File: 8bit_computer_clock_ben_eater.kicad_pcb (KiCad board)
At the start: 2 copper layers, 28 parts, among them SW1 Step, SW2 Switch, SW3 Halt, U1 LMC555xN, U2 LMC555xN, U3 LMC555xN, U4 74HC00, U5 74HC00

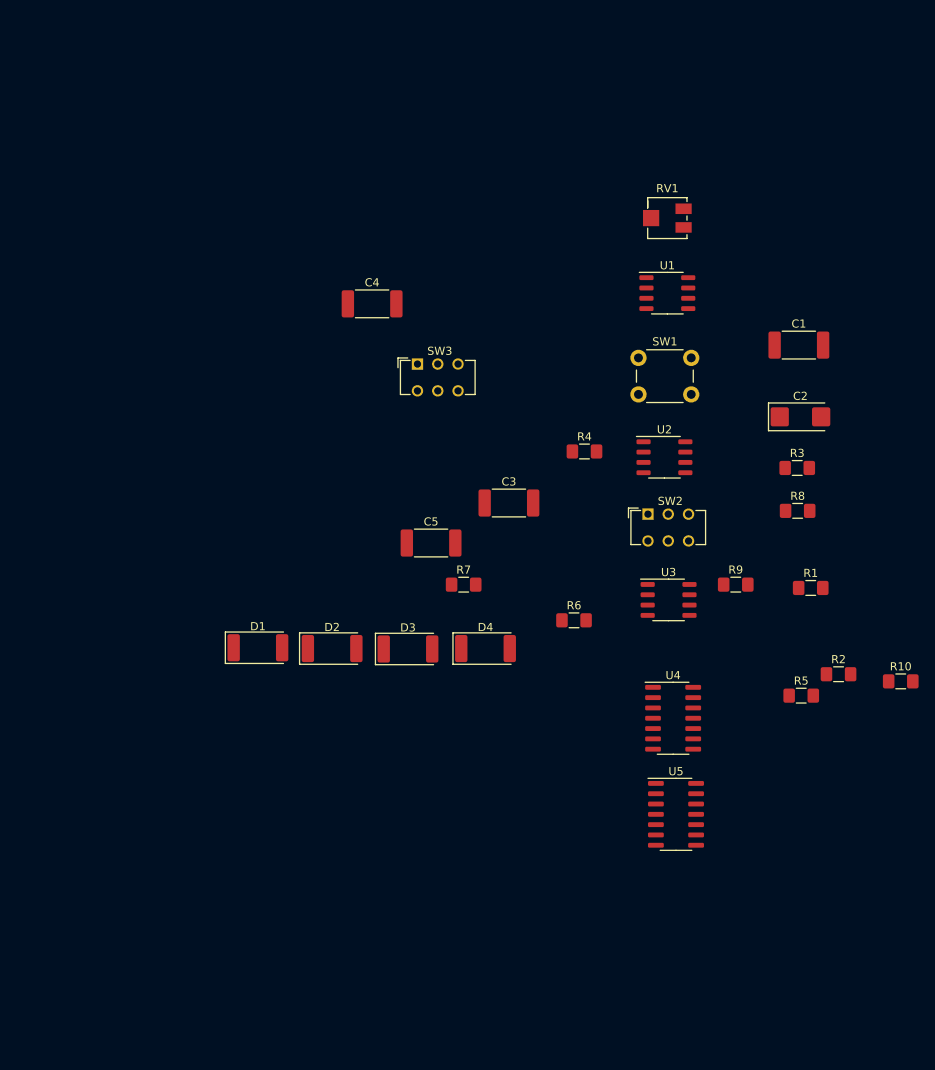
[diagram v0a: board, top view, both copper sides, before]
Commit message: New pcb layout. Added power connection.
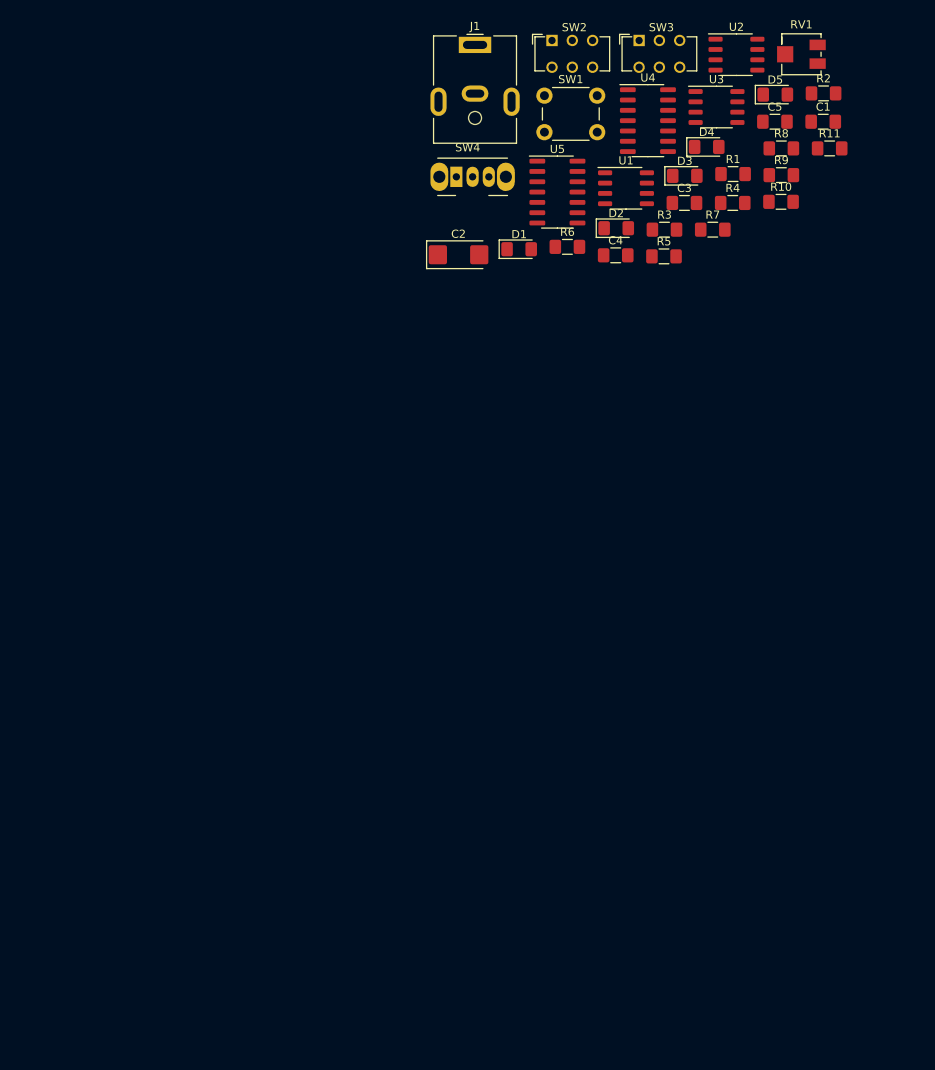
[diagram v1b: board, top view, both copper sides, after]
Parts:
- added D5: LED, LED_SMD:LED_1206_3216Metric_Pad1.42x1.75mm_HandSolder, F.Cu at (187.8, 30.5)
- added J1: Barrel_Jack_MountingPin, Connector_BarrelJack:BarrelJack_CUI_PJ-063AH_Horizontal, F.Cu at (150.8, 24.4)
- added R11: 1k, Resistor_SMD:R_1206_3216Metric_Pad1.42x1.75mm_HandSolder, F.Cu at (194.5, 37.1)
- added SW4: SW_SPDT, Button_Switch_THT:SW_CuK_OS102011MA1QN1_SPDT_Angled, F.Cu at (148.5, 40.6)
- C1, C3, C4, C5: footprint Capacitor_SMD:C_2512_6332Metric_Pad1.52x3.35mm_HandSolder -> Capacitor_SMD:C_1206_3216Metric_Pad1.42x1.75mm_HandSolder
- D1, D2, D3, D4: footprint LED_SMD:LED_2512_6332Metric_Pad1.52x3.35mm_HandSolder -> LED_SMD:LED_1206_3216Metric_Pad1.42x1.75mm_HandSolder
- moved U5 78.0 mm to (161.0, 42.5)
- moved U4 73.7 mm to (172.1, 33.7)
- moved R2 71.6 mm to (193.7, 30.4)
- moved D4 67.5 mm to (179.4, 37.0)
- moved D3 67.5 mm to (176.7, 40.5)
- moved C5 67.0 mm to (187.8, 33.8)
- moved D2 62.5 mm to (168.2, 47.0)
- moved U3 61.0 mm to (180.6, 32.0)
- moved R10 60.9 mm to (188.5, 43.7)
- moved SW2 59.5 mm to (160.3, 23.8)
- moved D1 58.7 mm to (156.2, 49.6)
- moved R5 56.7 mm to (174.1, 50.4)
- moved R7 53.4 mm to (180.1, 47.1)
- moved R1 51.9 mm to (182.6, 40.3)
- moved R9 50.8 mm to (188.5, 40.4)
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
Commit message: Changed all footprints to SMD/SMT. Used a 556 instead of two 555. Beginning of a PCB.
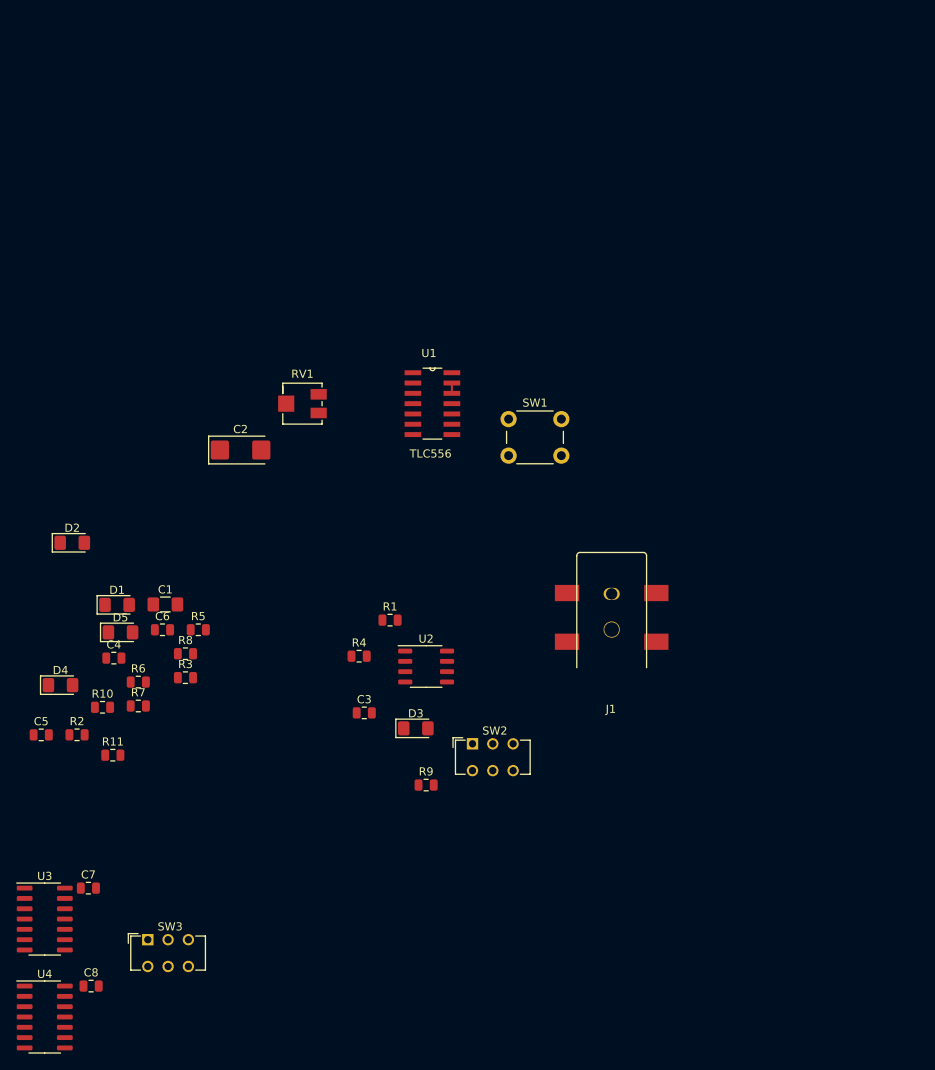
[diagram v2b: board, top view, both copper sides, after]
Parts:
- removed SW4: SW_SPDT, Button_Switch_THT:SW_CuK_OS102011MA1QN1_SPDT_Angled
- removed U5: 74HC00, Package_SO:SOIC-14_3.9x8.7mm_P1.27mm
- added C6: 0.1uF, Capacitor_SMD:C_0805_2012Metric, F.Cu at (112.3, 96.4)
- added C7: 0.1uF, Capacitor_SMD:C_0805_2012Metric, F.Cu at (103.2, 128.3)
- added C8: 0.1uF, Capacitor_SMD:C_0805_2012Metric, F.Cu at (103.5, 140.3)
- C1: value 10nF -> 100nF
- C3: value 100nF -> 10nF; footprint Capacitor_SMD:C_1206_3216Metric_Pad1.42x1.75mm_HandSolder -> Capacitor_SMD:C_0805_2012Metric
- C4, C5: footprint Capacitor_SMD:C_1206_3216Metric_Pad1.42x1.75mm_HandSolder -> Capacitor_SMD:C_0805_2012Metric
- J1: value Barrel_Jack_MountingPin -> Barrel_Jack_Switch; footprint Connector_BarrelJack:BarrelJack_CUI_PJ-063AH_Horizontal -> grotto:Barrel Jack RS Pro DC Socket 2.5mm - SMT
- R1, R3, R4, R9: footprint Resistor_SMD:R_1206_3216Metric_Pad1.42x1.75mm_HandSolder -> Resistor_SMD:R_0805_2012Metric
- R10, R2: value 220 -> 1k; footprint Resistor_SMD:R_1206_3216Metric_Pad1.42x1.75mm_HandSolder -> Resistor_SMD:R_0805_2012Metric
- R11, R7, R8: value 1k -> 220; footprint Resistor_SMD:R_1206_3216Metric_Pad1.42x1.75mm_HandSolder -> Resistor_SMD:R_0805_2012Metric
- R5: value 1M -> 1k; footprint Resistor_SMD:R_1206_3216Metric_Pad1.42x1.75mm_HandSolder -> Resistor_SMD:R_0805_2012Metric
- R6: value 220 -> 1M; footprint Resistor_SMD:R_1206_3216Metric_Pad1.42x1.75mm_HandSolder -> Resistor_SMD:R_0805_2012Metric
- RV1: value 100k -> 1M
- U1: value LMC555xN -> TLC556; footprint Package_SO:SO-8_3.9x4.9mm_P1.27mm -> grotto:SOIC127P600X175-14N
- U3: value LMC555xN -> 74HC00; footprint Package_SO:SO-8_3.9x4.9mm_P1.27mm -> Package_SO:SOIC-14_3.9x8.7mm_P1.27mm
- moved U4 133.1 mm to (97.8, 144.1)
- moved U3 129.8 mm to (97.8, 132.1)
- moved SW3 126.2 mm to (110.5, 134.6)
- moved R2 121.3 mm to (101.8, 109.4)
- moved C5 117.8 mm to (97.4, 109.4)
- moved R11 115.7 mm to (106.2, 111.9)
- moved D5 104.4 mm to (107.1, 96.8)
- moved R10 104.2 mm to (104.9, 106.0)
- moved D4 103.6 mm to (99.7, 103.3)
- moved C1 100.5 mm to (112.7, 93.3)
- moved R8 96.3 mm to (115.1, 99.4)
- moved R7 91.9 mm to (109.3, 105.8)
- moved SW2 87.2 mm to (150.5, 110.5)
- moved R9 87.0 mm to (144.8, 115.6)
- moved U2 84.5 mm to (144.8, 101.0)
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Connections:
- C1 pad 1: Net-(C1-Pad1) -> GND
- C1 pad 2: GND -> /THRESB
- C3 pad 1: GND -> /CV
- C3 pad 2: Net-(C3-Pad2) -> GND
- C4 pad 1: Net-(C4-Pad1) -> GND
- C4 pad 2: GND -> Net-(C4-Pad2)
- C5 pad 1: Net-(C5-Pad1) -> GND
- C5 pad 2: GND -> /CONTB
- D1 pad 1: Net-(D1-Pad1) -> GND
- D2 pad 2: Net-(D2-Pad2) -> /OUTB
- D3 pad 2: Net-(D3-Pad2) -> /Q
- D4 pad 2: Net-(D4-Pad2) -> VCC
- D5 pad 2: VCC -> Net-(D5-Pad2)
- J1 pad 1: /PWR_IN -> VCC
- R1 pad 2: Net-(R1-Pad2) -> /R
- R2 pad 1: Net-(D1-Pad1) -> VCC
- R2 pad 2: GND -> /TRIGB
- R3 pad 2: Net-(R1-Pad2) -> Net-(R3-Pad2)
- R4 pad 2: Net-(R4-Pad2) -> /TR
- R5 pad 2: Net-(C3-Pad2) -> Net-(R3-Pad1)
- R6 pad 1: GND -> /THRESB
- R6 pad 2: Net-(D2-Pad1) -> VCC
- R7 pad 1: VCC -> Net-(D1-Pad2)
- R8 pad 1: VCC -> Net-(D2-Pad1)
- R8 pad 2: Net-(R8-Pad2) -> GND
- RV1 pad 3: Net-(R3-Pad1) -> Net-(R3-Pad2)
- SW1 pad 2: Net-(R4-Pad2) -> /TRIGB
- SW2 pad 1: Net-(R8-Pad2) -> /TR
- SW2 pad 3: Net-(R7-Pad2) -> /R
- U1 pad 1: GND -> Net-(R3-Pad1)
- U1 pad 3: Net-(D1-Pad2) -> Net-(C4-Pad2)
- U1 pad 5: Net-(C1-Pad1) -> Net-(R7-Pad2)
- U1 pad 7: Net-(R1-Pad2) -> GND
- U1 pad 8: VCC -> /TRIGB
- U2 pad 2: Net-(R4-Pad2) -> /TR
- U2 pad 3: Net-(D2-Pad2) -> /Q
- U2 pad 4: VCC -> /R
- U2 pad 5: Net-(C4-Pad1) -> /CV
- U2 pad 6: Net-(C3-Pad2) -> GND
- U2 pad 7: Net-(C3-Pad2) -> Net-(U2-Pad7)
- U3 pad 1: GND -> Net-(R7-Pad2)
- U3 pad 2: Net-(R8-Pad2) -> /Q
- U3 pad 3: Net-(D3-Pad2) -> Net-(U3-Pad3)
- U3 pad 4: Net-(R7-Pad2) -> /Q
- U3 pad 5: Net-(C5-Pad1) -> /Q
- U3 pad 6: GND -> Net-(U3-Pad12)
- U3 pad 7: Net-(U3-Pad7) -> GND
- U3 pad 8: VCC -> Net-(U3-Pad8)
- U4 pad 1: Net-(D1-Pad2) -> Net-(U3-Pad3)
- U4 pad 10: Net-(SW3-Pad2) -> Net-(U4-Pad10)
- U4 pad 12: Net-(U4-Pad12) -> GND
- U4 pad 13: Net-(D2-Pad2) -> GND
- U4 pad 14: (no net) -> VCC
- U4 pad 2: Net-(D3-Pad2) -> Net-(U3-Pad11)
- U4 pad 4: Net-(D3-Pad2) -> Net-(U4-Pad3)
- U4 pad 5: Net-(D3-Pad2) -> Net-(U3-Pad8)
- U4 pad 6: Net-(U4-Pad12) -> Net-(U4-Pad10)
- U4 pad 7: (no net) -> GND
- U4 pad 8: Net-(U4-Pad8) -> Net-(D5-Pad2)
- U4 pad 9: Net-(SW3-Pad2) -> Net-(U4-Pad10)
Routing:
- net /THRESB: track 0.00 -> 1.27 mm

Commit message: PCB finished.
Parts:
- removed D4: LED, LED_SMD:LED_1206_3216Metric_Pad1.42x1.75mm_HandSolder
- removed R10: 1k, Resistor_SMD:R_0805_2012Metric
- added C10: 100nF, Capacitor_SMD:C_0805_2012Metric, F.Cu at (162.3, 68.2)
- added C11: 0.1uF, Capacitor_SMD:C_0805_2012Metric, F.Cu at (166.4, 93.9)
- added C9: 100uF, Capacitor_Tantalum_SMD:CP_EIA-3528-12_Kemet-T, F.Cu at (162.3, 73.3)
- added TP1: CLK, Connector_PinHeader_2.54mm:PinHeader_1x01_P2.54mm_Vertical, F.Cu at (168.7, 116.6)
- C1: footprint Capacitor_SMD:C_1206_3216Metric_Pad1.42x1.75mm_HandSolder -> Capacitor_SMD:C_0805_2012Metric
- C2: footprint Capacitor_Tantalum_SMD:CP_EIA-6032-28_Kemet-C_Pad2.25x2.35mm_HandSolder -> Capacitor_Tantalum_SMD:CP_EIA-3528-12_Kemet-T
- D1, D2, D3, D5: footprint LED_SMD:LED_1206_3216Metric_Pad1.42x1.75mm_HandSolder -> LED_SMD:LED_0805_2012Metric
- RV1: footprint Potentiometer_SMD:Potentiometer_Bourns_3214J_Horizontal -> Potentiometer_SMD:Potentiometer_Bourns_3214W_Vertical
- SW1: footprint Button_Switch_THT:SW_PUSH_6mm_H4.3mm -> Button_Switch_SMD:Panasonic_EVQPUK_EVQPUB
- SW2, SW3: footprint Button_Switch_THT:SW_CuK_JS202011CQN_DPDT_Straight -> grotto:G3T12
- moved C5 78.0 mm to (171.6, 85.6), turned to 180 degrees
- moved U3 72.5 mm to (166.8, 109.9)
- moved D2 70.5 mm to (171.6, 87.6), turned to 180 degrees
- moved SW3 70.2 mm to (176.3, 110.2)
- moved C7 69.9 mm to (168.7, 104.1), turned to 180 degrees
- moved U4 69.8 mm to (158.6, 109.9)
- moved R2 68.5 mm to (167.8, 91.2)
- moved C8 67.0 mm to (159.9, 104.1), turned to 180 degrees
- moved R6 66.0 mm to (171.6, 81.0)
- moved C1 59.9 mm to (171.7, 83.1), turned to 180 degrees
- moved C6 59.2 mm to (168.9, 79.0), turned to 90 degrees
- moved R8 57.3 mm to (171.6, 89.7), turned to 180 degrees
- moved D5 56.7 mm to (160.6, 115.6)
- moved C4 56.2 mm to (160.3, 84.3)
- moved R3 55.8 mm to (166.2, 79.8)
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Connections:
- net Net-(C4-Pad2) renamed /CONTA
- net Net-(R3-Pad1) renamed /DISCHA
- net Net-(R7-Pad2) renamed /OUTA
- C2 pad 1: Net-(C2-Pad1) -> /THRESHA
- RV1 pad 1: GND -> /THRESHA
- RV1 pad 2: Net-(C2-Pad1) -> Net-(R3-Pad2)
- RV1 pad 3: Net-(R3-Pad2) -> Net-(RV1-Pad3)
- U1 pad 2: Net-(C2-Pad1) -> /THRESHA
- U1 pad 6: Net-(C2-Pad1) -> /THRESHA
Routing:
- net GND: track 0.00 -> 61.9 mm, vias 0 -> 18
- net /OUTB: track 0.00 -> 29.0 mm
- net /OUTA: track 0.00 -> 27.5 mm
- net /THRESHA: track 0.00 -> 24.1 mm
- net /Q: track 0.00 -> 20.0 mm
- net /TRIGB: track 0.00 -> 18.8 mm
- net Net-(U3-Pad11): track 0.00 -> 18.1 mm
- net Net-(U3-Pad8): track 0.00 -> 17.5 mm
- net /TR: track 0.00 -> 15.9 mm
- net /R: track 0.00 -> 14.6 mm
- net Net-(R3-Pad2): track 0.00 -> 14.5 mm
- net Net-(D5-Pad2): track 0.00 -> 9.65 mm
- net Net-(U3-Pad3): track 0.00 -> 9.24 mm
- net Net-(U3-Pad12): track 0.00 -> 6.53 mm
- net Net-(U4-Pad10): track 0.00 -> 6.22 mm
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- added copper zone on B.Cu, net GND
- added copper zone on F.Cu, net VCC
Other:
- board outline added: 26.8 x 56.9 mm
- net class Default: clearance 0.2 -> 0.1524; trace_width 0.25 -> 0.1524; via_drill 0.4 -> 0.254
- rule trace_clearance: 0.2 -> 0.1524
- rule trace_min: 0.2 -> 0.1524
- rule via_min_drill: 0.3 -> 0.254

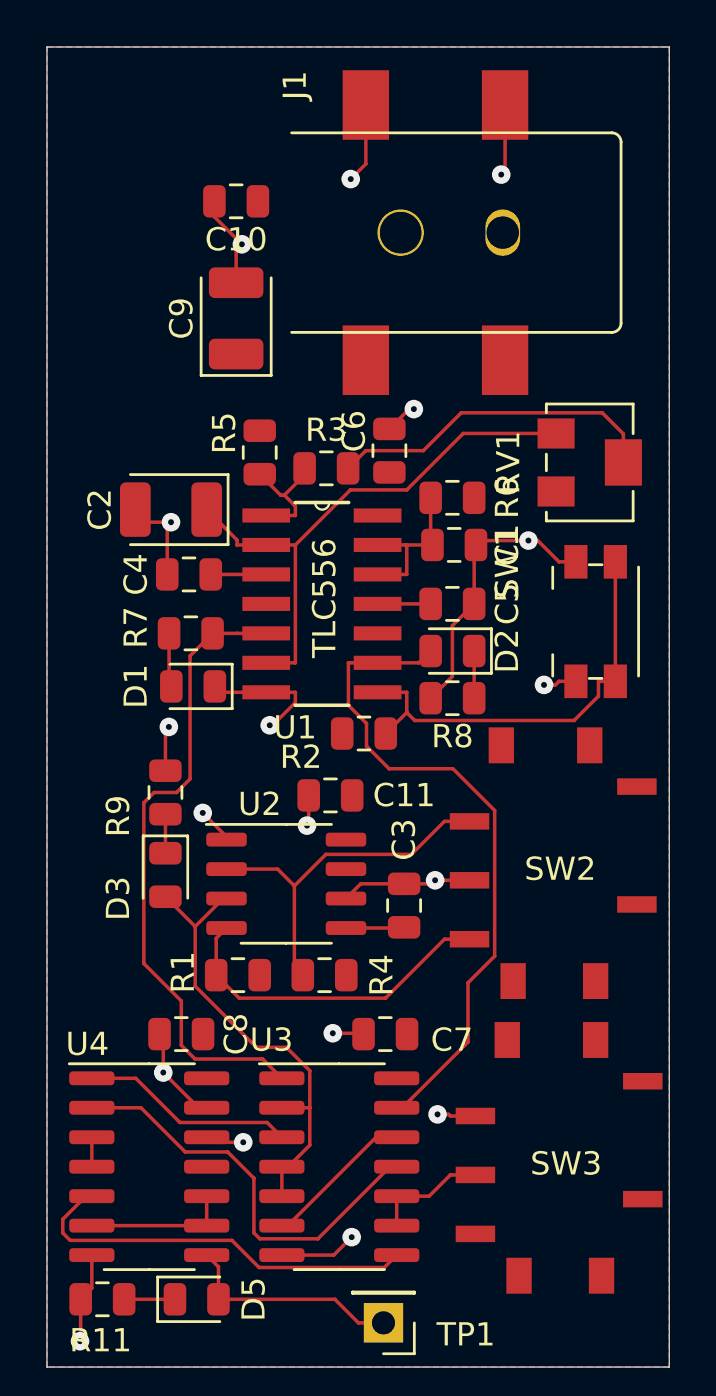
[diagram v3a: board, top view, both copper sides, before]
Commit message: Fixed traces autorouter failed to route. Ordered PCB with OSHPark.
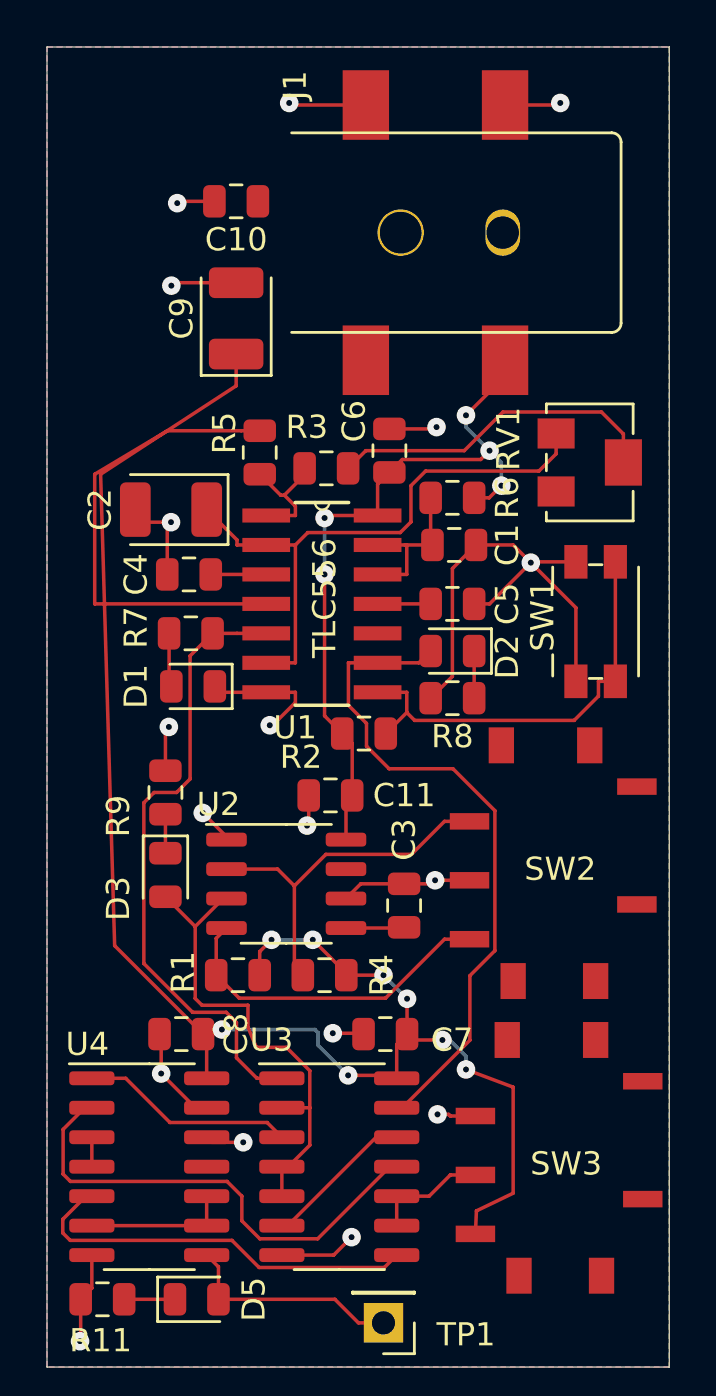
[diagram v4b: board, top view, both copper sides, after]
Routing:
- net VCC: track 0.00 -> 123.2 mm, vias 0 -> 13
- net GND: track 61.9 -> 69.7 mm
- net Net-(U3-Pad11): track 18.1 -> 21.0 mm
- net /THRESHA: track 24.1 -> 25.6 mm
- net /Q: track 20.0 -> 21.0 mm
